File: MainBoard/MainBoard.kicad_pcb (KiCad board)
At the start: 4 copper layers, 35 x 35 mm, 78 parts, among them IC1 MAX30102, IC2 TESEO-LIV3F, J1 PV IN, J2 Conn_Coaxial, J3 Conn_01x30_Female, J4 Conn_Coaxial, J6 Conn_01x04, SW1 SW_DIP_x01, SW2 SW_DIP_x01, SW3 SW_DIP_x01, U1 STM32WB30CEU5A, U2 MAX20361AEWC+, U3 DLF162500LT-5028A1, U4 LSM9DS1, U5 TPS63001, U6 CAT24M01Y, U7 CAT24M01Y, U8 CAT24M01Y, U9 CAT24M01Y, Y1 32 kHz, Y2 32 MHz

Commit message: route entire damn thing in one sitting
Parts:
- moved Y2 0.72 mm to (129.7, 34.9)
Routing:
- net +3V3: track 39.4 -> 214.5 mm, vias 10 -> 32
- net SCL: track 1.29 -> 85.8 mm, vias 2 -> 9
- net SDA: track 1.48 -> 82.1 mm, vias 2 -> 7
- net GND: track 34.7 -> 100.4 mm, vias 5 -> 34
- net Net-(IC2-Pad4): track 0.80 -> 33.9 mm, vias 1 -> 2
- net Net-(R3-Pad1): track 9.39 -> 41.1 mm, vias 1 -> 2
- net Net-(IC2-Pad5): track 0.80 -> 30.7 mm, vias 1 -> 2
- net TX: track 0.80 -> 30.2 mm
- net Net-(R4-Pad1): track 6.78 -> 35.4 mm, vias 1 -> 2
- net Net-(TP2-Pad1): track 0.80 -> 26.4 mm
- net Net-(R5-Pad1): track 7.44 -> 30.9 mm, vias 1 -> 2
- net Net-(JP5-Pad1): track 0.00 -> 22.2 mm, vias 0 -> 1
- net Net-(TP1-Pad1): track 0.80 -> 20.7 mm
- net RX: track 0.80 -> 16.0 mm
- net Net-(BT1-Pad1): track 21.1 -> 35.7 mm, vias 1 -> 4
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- added copper zone on In2.Cu, net GND

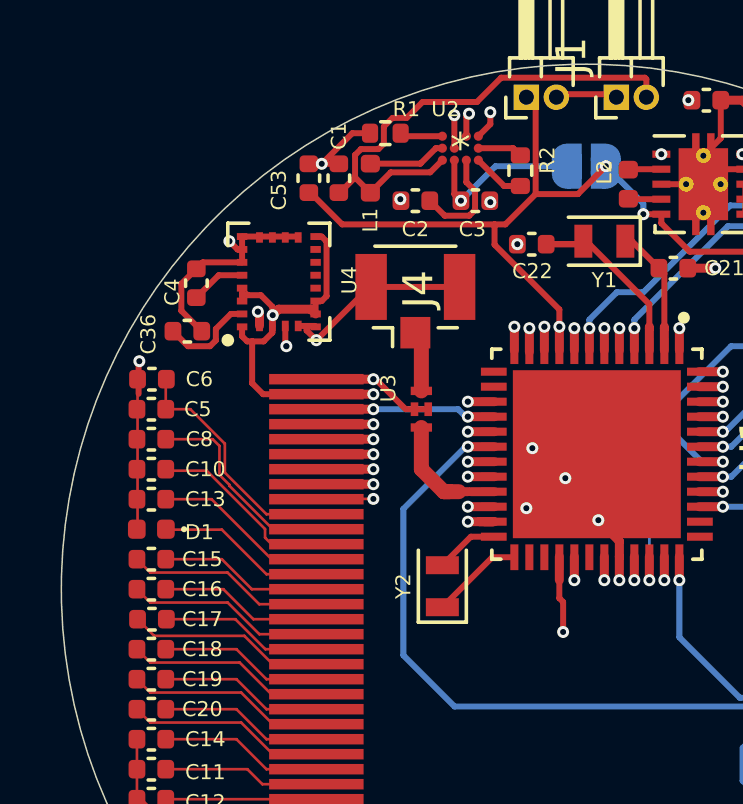
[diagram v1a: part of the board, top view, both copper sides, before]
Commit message: add crystal, pour ground plane
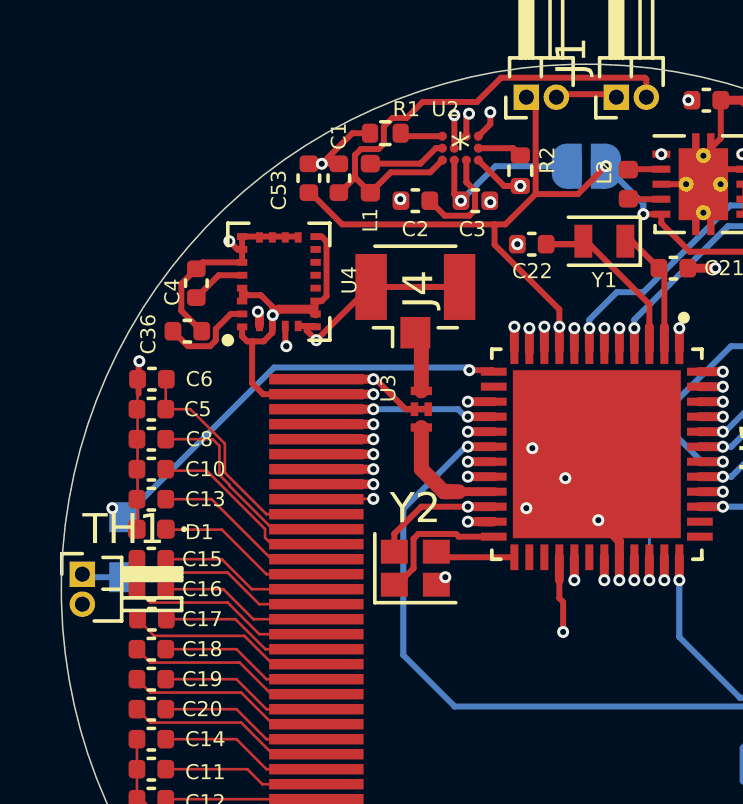
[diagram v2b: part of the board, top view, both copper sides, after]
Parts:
- added TH1: Thermistor, Connector_PinHeader_1.00mm:PinHeader_1x02_P1.00mm_Horizontal, F.Cu at (117.7, 34.5)
- added TP8: Buzzer, TestPoint:TestPoint_Pad_1.0x1.0mm, B.Cu at (119.1, 32.6)
- added TP9: BuzzerGnd, TestPoint:TestPoint_Pad_1.0x1.0mm, B.Cu at (119.1, 34.6)
- Y2: value 32 MHz -> Crystal_GND24; footprint Crystal:Crystal_SMD_2012-2Pin_2.0x1.2mm -> Crystal:Crystal_SMD_2016-4Pin_2.0x1.6mm
- moved Y2 1.08 mm to (128.8, 34.3), turned to 0 degrees
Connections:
- U1 pad 13: (no net) -> Net-(TP8-Pad1)
- Y2 pad 1: Net-(U1-Pad25) -> Net-(U1-Pad24)
- Y2 pad 2: Net-(U1-Pad24) -> GND
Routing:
- net Net-(R2-Pad1): track 1.76 -> 22.2 mm, vias 0 -> 1
- net Net-(TP8-Pad1): track 0.00 -> 14.4 mm, vias 0 -> 2
- net GND: track 100.4 -> 105.3 mm, vias 34 -> 35
- net Net-(U1-Pad24): track 2.11 -> 4.63 mm

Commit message: many, many things :)
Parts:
- removed C21, C22: Loading, Capacitor_SMD:C_0402_1005Metric
- removed C36: 100uF, Capacitor_SMD:C_0402_1005Metric
- removed C4: 10nF, Capacitor_SMD:C_0402_1005Metric
- removed C53, C55, C56: 10uF, Capacitor_SMD:C_0402_1005Metric
- removed C54: 0.1uF, Capacitor_SMD:C_0402_1005Metric
- removed IC2: TESEO-LIV3F, libs:SON110P970X1010X230-18N
- removed J1: PV IN, Connector_PinHeader_1.00mm:PinHeader_1x02_P1.00mm_Horizontal
- removed J2, J4: Conn_Coaxial, Connector_Coaxial:U.FL_Hirose_U.FL-R-SMT-1_Vertical
- removed JP2: WP1, Jumper:SolderJumper-2_P1.3mm_Open_Pad1.0x1.5mm
- removed JP3: WP3, Jumper:SolderJumper-2_P1.3mm_Open_Pad1.0x1.5mm
- removed JP4: WP2, Jumper:SolderJumper-2_P1.3mm_Open_Pad1.0x1.5mm
- removed JP5: WP4, Jumper:SolderJumper-2_P1.3mm_Open_Pad1.0x1.5mm
- removed L2: 1uH, Inductor_SMD:L_0402_1005Metric
- removed TH1: Thermistor, Connector_PinHeader_1.00mm:PinHeader_1x02_P1.00mm_Horizontal
- removed U3: DLF162500LT-5028A1, libs:DLF162500LT
- removed U4: LSM9DS1, Package_LGA:LGA-24L_3x3.5mm_P0.43mm
- removed U5: TPS63001, Package_SON:Texas_DRC0010J_ThermalVias
- removed U6, U7, U8, U9: CAT24M01Y, Package_SO:TSSOP-8_4.4x3mm_P0.65mm
- removed Y1: 32 kHz, Crystal:Crystal_SMD_2012-2Pin_2.0x1.2mm
- removed Y2: Crystal_GND24, Crystal:Crystal_SMD_2016-4Pin_2.0x1.6mm
- added BZ1: Buzzer, libs:PB9.11-5v, B.Cu at (120.0, 38.5)
- added R7: 2k, Resistor_SMD:R_0402_1005Metric, F.Cu at (149.0, 43.5)
- added R8: 2k, Resistor_SMD:R_0402_1005Metric, F.Cu at (122.5, 50.0)
- BT1: footprint Connector_PinHeader_1.00mm:PinHeader_1x02_P1.00mm_Horizontal -> Connector_PinHeader_1.00mm:PinHeader_1x02_P1.00mm_Vertical
- C1: value 1uF -> 4.5uF
- C2, C3: value 1uF -> 5.7k
- J6: moved to B.Cu
- JP1: value PV EN -> WP; footprint Jumper:SolderJumper-2_P1.3mm_Open_RoundedPad1.0x1.5mm -> Jumper:SolderJumper-2_P1.3mm_Open_Pad1.0x1.5mm; moved to F.Cu
- L1: value INDUCTOR -> 1uH; footprint Inductor_SMD:L_0402_1005Metric -> Inductor_SMD:L_0805_2012Metric
- R1: value 5K -> 2k
- R2: value R_US -> 2k
- R6: value 100 -> 2k
- TP1: value TestPoint -> RST
- TP2: value JTMS_SWDIO -> IO12
- TP3: value JTCK_SWCLK -> IO14
- TP4: value JTDI -> BOOT0
- TP5: value JTDO -> IO13
- TP6: value NJTRST -> IO15
- TP7: value BOOT0 -> BOOT1
- TP8: value Buzzer -> STX
- TP9: value BuzzerGnd -> SRX
- U1: value STM32WB30CEU5A -> ESP32-WROOM-32; footprint libs:STM32WB30CEU5A -> RF_Module:ESP32-WROOM-32
- U2: value MAX20361AEWC+ -> ADP2108AUJ-3.3; footprint libs:MAX20361AEWC&plus_ -> Package_TO_SOT_SMD:TSOT-23-5
- moved BT1 34.4 mm to (143.5, 51.2), turned to 135 degrees
- moved R1 33.1 mm to (142.5, 49.5)
- moved C1 32.4 mm to (146.0, 47.0), turned to 0 degrees
- moved R6 31.3 mm to (122.5, 45.0), turned to 0 degrees
- moved TP8 30.8 mm to (147.5, 44.5), turned to 0 degrees
- moved JP1 30.1 mm to (121.5, 48.0)
- moved TP9 29.8 mm to (145.5, 48.5), turned to 0 degrees
- moved U2 28.7 mm to (146.5, 44.0), turned to 90 degrees
- moved TP10 27.7 mm to (127.5, 52.0)
- moved L1 27.2 mm to (146.5, 40.5), turned to 0 degrees
- moved R2 26.7 mm to (144.0, 45.0)
- moved C3 25.2 mm to (149.5, 39.0)
- moved C7 25.1 mm to (145.0, 31.0)
- moved C2 25.0 mm to (148.5, 37.5), turned to 0 degrees
- moved C9 24.6 mm to (145.5, 34.5)
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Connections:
- C1 pad 1: Net-(C1-Pad1) -> Net-(BT1-Pad1)
- C2 pad 1: Net-(C2-Pad1) -> +3V3
- C2 pad 2: GND -> SDA
- C3 pad 1: Net-(C3-Pad1) -> +3V3
- C3 pad 2: GND -> SCL
- IC1 pad 1: (no net) -> Net-(IC1-Pad1)
- IC1 pad 13: (no net) -> Net-(IC1-Pad13)
- IC1 pad 14: (no net) -> Net-(IC1-Pad14)
- IC1 pad 5: (no net) -> Net-(IC1-Pad5)
- IC1 pad 6: (no net) -> Net-(IC1-Pad6)
- IC1 pad 7: (no net) -> Net-(IC1-Pad7)
- IC1 pad 8: (no net) -> Net-(IC1-Pad8)
- J3 pad 30: (no net) -> Net-(J3-Pad30)
- JP1 pad 1: Net-(C3-Pad1) -> Net-(JP1-Pad1)
- JP1 pad 2: Net-(BT1-Pad1) -> GND
- L1 pad 1: Net-(C1-Pad1) -> Net-(L1-Pad1)
- L1 pad 2: Net-(L1-Pad2) -> +3V3
- R1 pad 1: GND -> +3V3
- R1 pad 2: Net-(R1-Pad2) -> Net-(IC1-Pad13)
- R6 pad 1: Net-(BT1-Pad1) -> +3V3
- R6 pad 2: Net-(C54-Pad1) -> Net-(R2-Pad1)
- TP1 pad 1: Net-(TP1-Pad1) -> Net-(R2-Pad2)
- TP4 pad 1: Net-(TP4-Pad1) -> Net-(R7-Pad1)
- TP7 pad 1: Net-(TP7-Pad1) -> Net-(R8-Pad2)
- TP9 pad 1: GND -> Net-(TP9-Pad1)
- U1 pad 1: +3V3 -> GND
- U1 pad 10: SPI1-SCK -> Net-(J3-Pad5)
- U1 pad 11: Net-(IC2-Pad4) -> Net-(J3-Pad6)
- U1 pad 12: Net-(IC2-Pad5) -> Net-(J3-Pad7)
- U1 pad 13: Net-(TP8-Pad1) -> Net-(TP3-Pad1)
- U1 pad 14: (no net) -> Net-(TP2-Pad1)
- U1 pad 15: Net-(J3-Pad9) -> GND
- U1 pad 16: SPI1-MOSI -> Net-(TP5-Pad1)
- U1 pad 17: Net-(J3-Pad8) -> Net-(U1-Pad17)
- U1 pad 18: TX -> Net-(U1-Pad18)
- U1 pad 19: Net-(J3-Pad7) -> Net-(U1-Pad19)
- U1 pad 2: Net-(C21-Pad1) -> +3V3
- U1 pad 20: +3V3 -> Net-(U1-Pad20)
- U1 pad 22: GND -> Net-(U1-Pad22)
- U1 pad 23: +3V3 -> Net-(TP6-Pad1)
- U1 pad 24: Net-(U1-Pad24) -> Net-(R8-Pad2)
- U1 pad 25: Net-(U1-Pad25) -> Net-(R7-Pad1)
- U1 pad 26: (no net) -> Net-(R5-Pad1)
- U1 pad 27: (no net) -> Net-(U1-Pad27)
- U1 pad 28: Net-(J3-Pad5) -> Net-(U1-Pad28)
- U1 pad 29: Net-(J3-Pad6) -> Net-(U1-Pad29)
- U1 pad 3: Net-(C22-Pad1) -> Net-(R2-Pad1)
- U1 pad 30: (no net) -> SPI1-SCK
- U1 pad 31: +3V3 -> SPI1-MISO
- U1 pad 32: GND -> Net-(U1-Pad32)
- U1 pad 33: +3V3 -> SDA
- U1 pad 34: +3V3 -> Net-(TP9-Pad1)
- U1 pad 35: +3V3 -> Net-(TP8-Pad1)
- U1 pad 36: RX -> SCL
- U1 pad 37: (no net) -> SPI1-MOSI
- U1 pad 38: (no net) -> GND
- U1 pad 39: Net-(TP2-Pad1) -> GND
- U1 pad 4: Net-(TP7-Pad1) -> Net-(BZ1-Pad2)
- U1 pad 5: SCL -> Net-(BT1-Pad1)
- U1 pad 6: SDA -> Net-(R4-Pad1)
- U1 pad 7: Net-(TP1-Pad1) -> Net-(R3-Pad1)
- U1 pad 8: +3V3 -> Net-(J3-Pad8)
- U1 pad 9: Net-(BT1-Pad1) -> Net-(J3-Pad9)
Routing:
- net +3V3: track 214.5 -> 79.0 mm, vias 32 -> 12
- net GND: track 105.3 -> 48.5 mm, vias 35 -> 14
- net SCL: track 85.8 -> 38.1 mm, vias 9 -> 2
- net SDA: track 82.1 -> 34.7 mm, vias 7 -> 2
- net Net-(IC2-Pad4): track 33.9 -> 0.00 mm, vias 2 -> 0
- net Net-(R2-Pad1): track 22.2 -> 52.9 mm, vias 1 -> 2
- net Net-(IC2-Pad5): track 30.7 -> 0.00 mm, vias 2 -> 0
- net TX: track 30.2 -> 0.00 mm, vias 1 -> 0
- net Net-(R8-Pad2): track 0.00 -> 27.9 mm, vias 0 -> 2
- net Net-(TP9-Pad1): track 0.00 -> 23.5 mm, vias 0 -> 1
- net Net-(JP5-Pad1): track 22.2 -> 0.00 mm, vias 1 -> 0
- net Net-(TP1-Pad1): track 20.7 -> 0.00 mm, vias 1 -> 0
- net Net-(TP5-Pad1): track 11.2 -> 31.6 mm
- net Net-(J3-Pad7): track 9.22 -> 28.1 mm
- net Net-(C1-Pad1): track 16.8 -> 0.00 mm
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- added copper zone on In2.Cu, net +3V3
- added copper zone on In1.Cu, net GND
- removed copper zone on In2.Cu, net GND
